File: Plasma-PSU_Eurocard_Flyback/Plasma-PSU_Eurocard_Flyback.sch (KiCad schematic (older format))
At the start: 21 parts

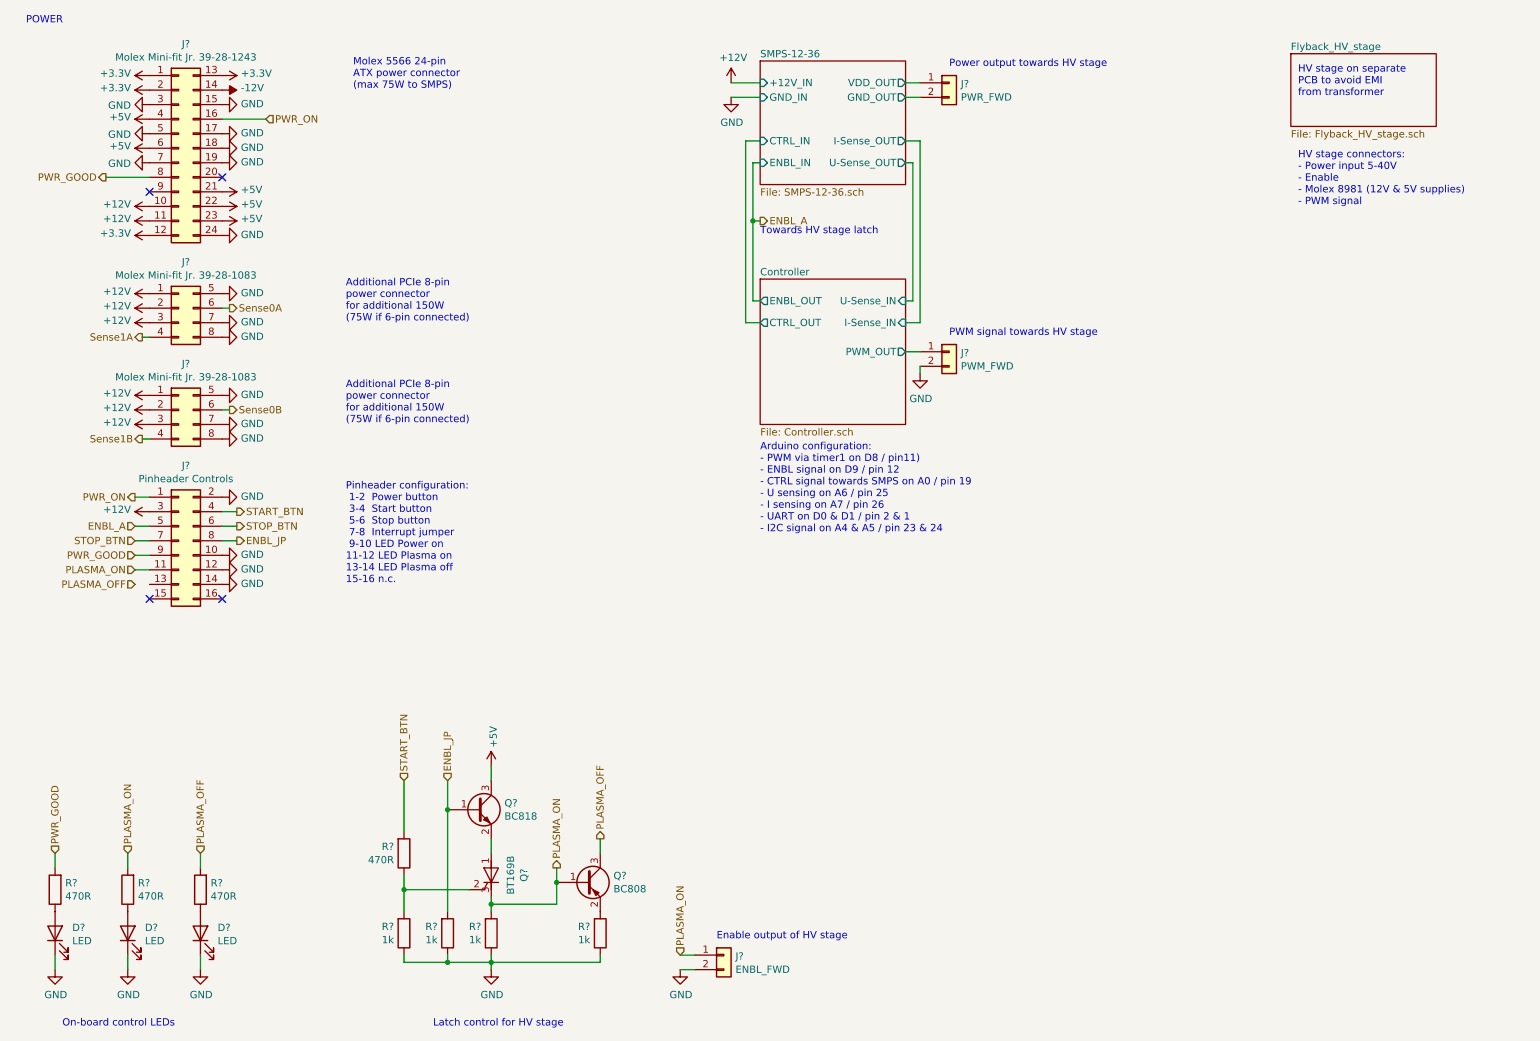
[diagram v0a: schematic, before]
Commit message: Block diagram, Connectivity, Isolation
- First page reservered for block diagram
- Connectors moved to separate sheet
- Opto-isolators for signal inputs on HV board
- Fuse added to SMPS
- Pinheader for Arduino pin-out, UART, I2C, SPI
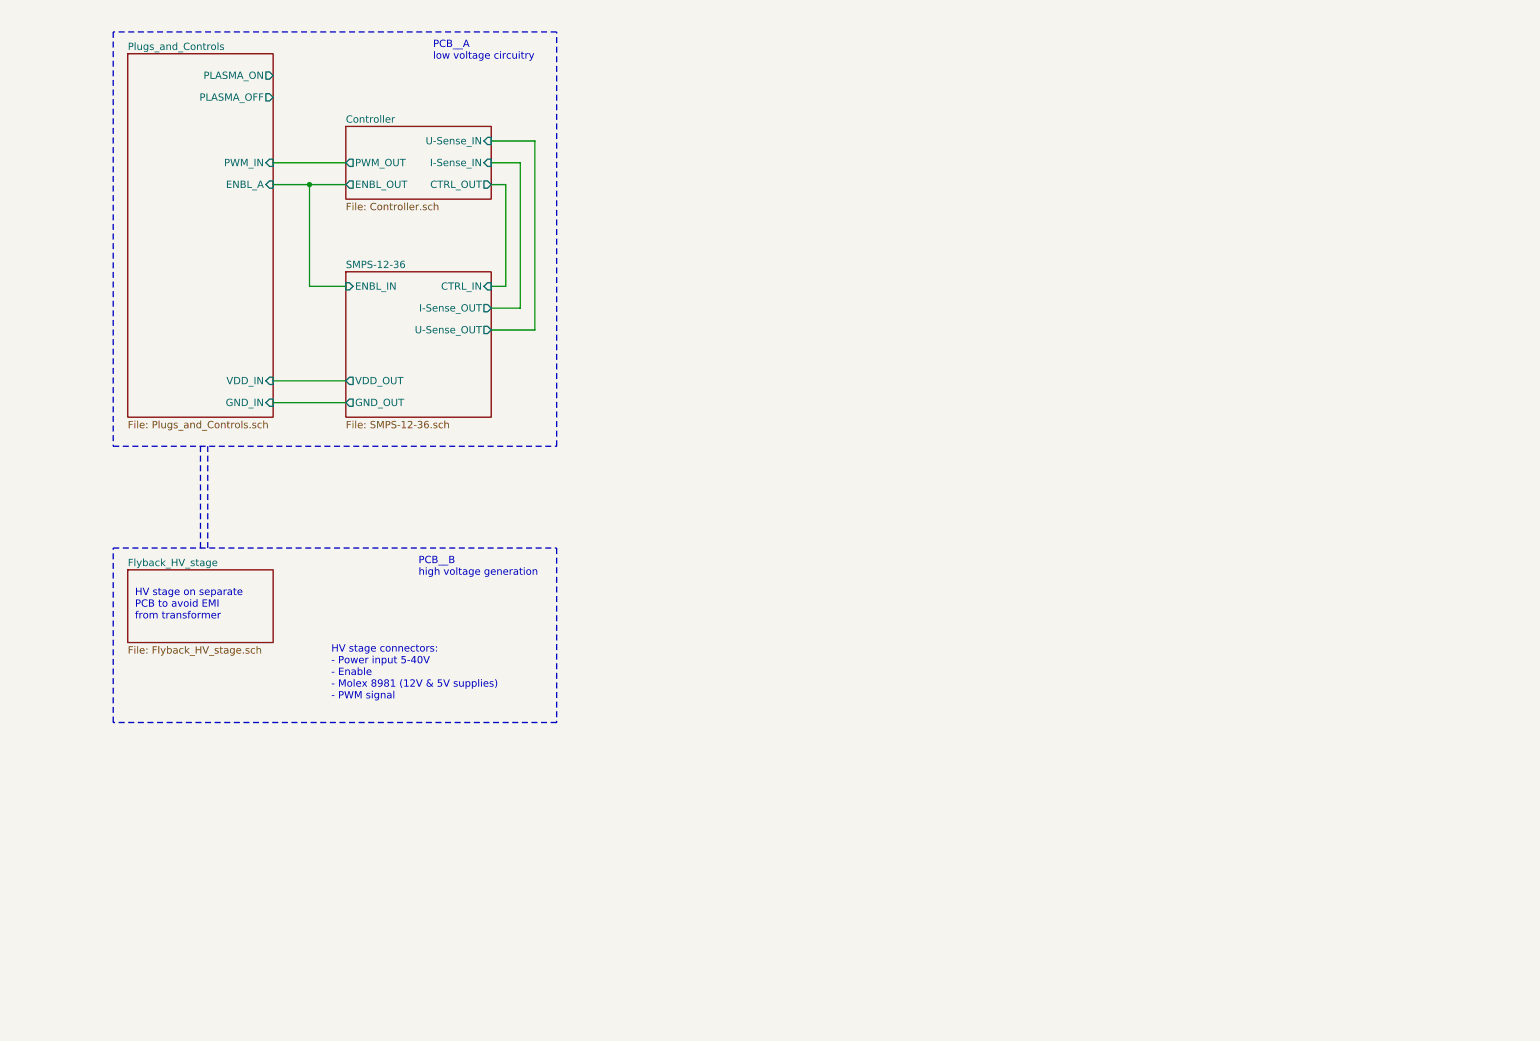
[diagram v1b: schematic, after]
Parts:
- removed D? (x3): LED, symbol Device:LED
- removed J?: Molex Mini-fit Jr. 39-28-1243, Connector_Molex:Molex_Mini-Fit_Jr_5566-24A_2x12_P4.20mm_Vertical, symbol Connector_Generic:Conn_02x12_Top_Bottom
- removed J? (x2): Molex Mini-fit Jr. 39-28-1083, Connector_Molex:Molex_Mini-Fit_Jr_5566-08A_2x04_P4.20mm_Vertical, symbol Connector_Generic:Conn_02x04_Top_Bottom
- removed J?: Pinheader Controls, Connector_PinHeader_2.54mm:PinHeader_2x08_P2.54mm_Vertical, symbol Connector_Generic:Conn_02x08_Odd_Even
- removed J?: PWR_FWD, symbol Connector_Generic:Conn_01x02
- removed J?: PWM_FWD, symbol Connector_Generic:Conn_01x02
- removed J?: ENBL_FWD, symbol Connector_Generic:Conn_01x02
- removed Q?: BT169B, Package_TO_SOT_THT:TO-92_Inline, symbol Triac_Thyristor:BT169B
- removed Q?: BC808, Package_TO_SOT_SMD:SOT-23, symbol Transistor_BJT:BC808
- removed Q?: BC818, Package_TO_SOT_SMD:SOT-23, symbol Transistor_BJT:BC818
- removed R? (x4): 1k, symbol Device:R
- removed R? (x4): 470R, symbol Device:R
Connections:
- no-connect marks 4 -> 0
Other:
- note added: "PCB__A\nlow voltage circuitry"
- note added: "PCB__B\nhigh voltage generation"
- note removed: "Additional PCIe 8-pin \npower connector\nfor additional 150W\n(75W if 6-pin connected)"
- note removed: "Arduino configuration:\n- PWM via timer1 on D8 / pin11)\n- ENBL signal on D9 / pin 12\n- CTRL signal towards SMPS on A0 / pin 19\n- U sensing on A6 / pin 25\n- I sensing on A7 / pin 26\n- UART on D0 & D1 / pin 2 & 1\n- I2C signal on A4 & A5 / pin 23 & 24"
- note removed: "Enable output of HV stage"
- note removed: "Latch control for HV stage"
- note removed: "Molex 5566 24-pin\nATX power connector\n(max 75W to SMPS)"
- note removed: "On-board control LEDs"
- note removed: "POWER"
- note removed: "PWM signal towards HV stage"
- note removed: "Pinheader configuration:\n 1-2 Power button\n 3-4 Start button\n 5-6 Stop button\n 7-8 Interrupt jumper\n 9-10 LED Power on\n11-12 LED Plasma on\n13-14 LED Plasma off\n15-16 n.c."
- note removed: "Power output towards HV stage"
- note removed: "Towards HV stage latch"

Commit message: Block diagram included
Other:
- note added: "12-36V\n0-15A"
- note added: "12V, 5V, GND"
- note added: "ARDUINO"
- note added: "ATX\nPOWER SUPPLY"
- note added: "BLOCK DIAGRAM"
- note added: "BOOST MODULE"
- note added: "DAC"
- note added: "FLYBACK\nDRIVER"
- note added: "HV FLYBACK\nTRANSFORMER"
- note added: "HV out"
- note added: "HV stage connectors:\n- Power input 5-40V\n- Enable\n- PWM signal"
- note added: "PCB A -- \nlow voltage circuits"
- note added: "PCB B -- \nhigh voltage generation"
- note added: "PWM (f,d%)"
- note added: "SOFT-START IC"
- note added: "sense U, I"
- note added: "set U"
- note removed: "HV stage connectors:\n- Power input 5-40V\n- Enable\n- Molex 8981 (12V & 5V supplies)\n- PWM signal"

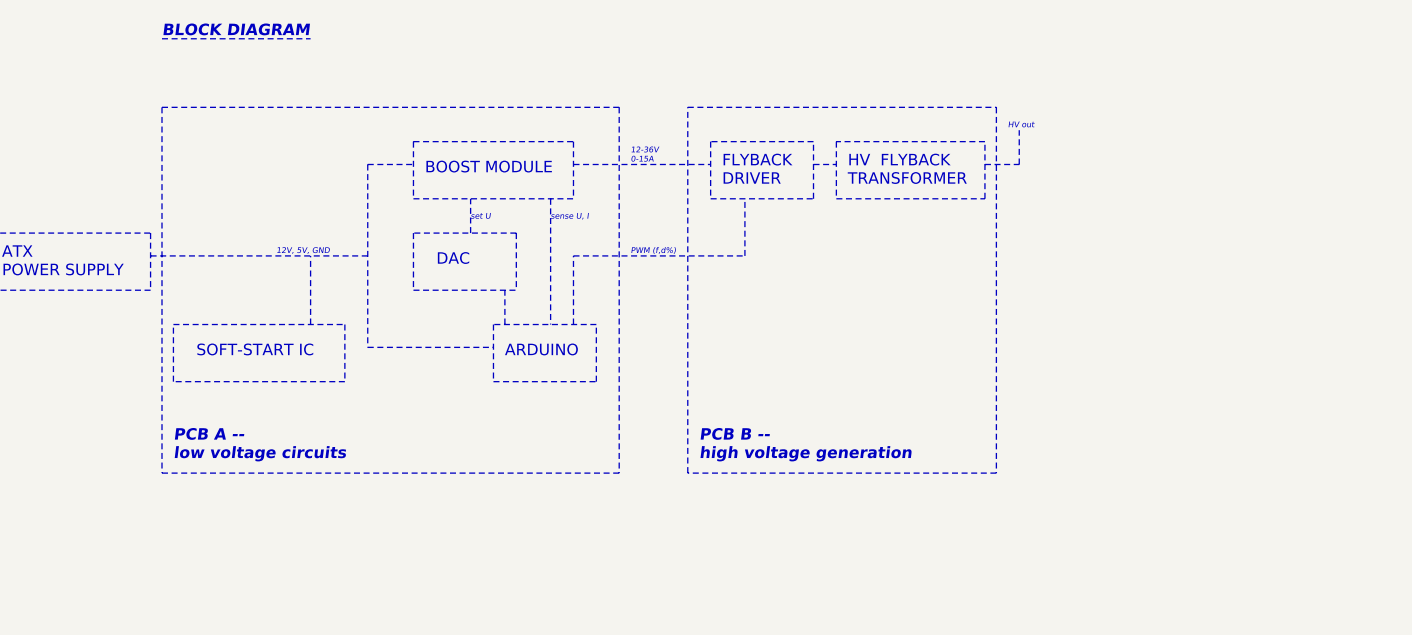
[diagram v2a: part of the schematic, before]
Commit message: Filters for sense signals
- RC filters on U-sense and I-sense included
- Block diagram refined
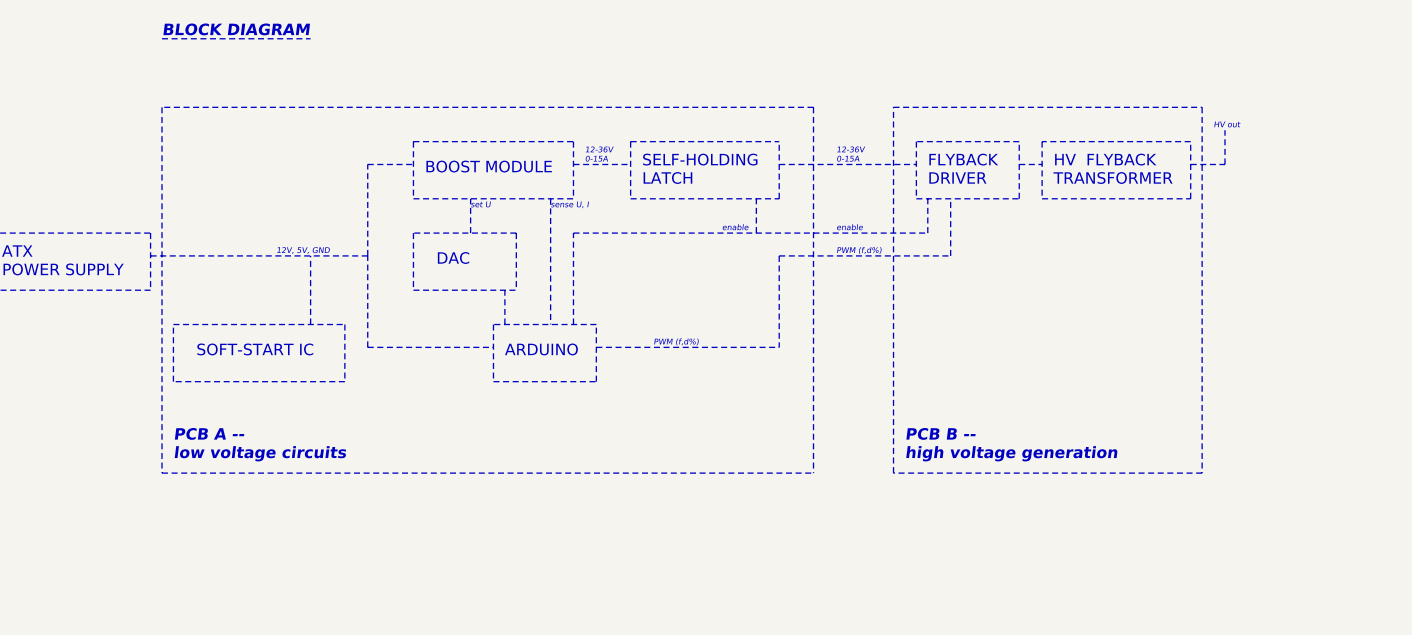
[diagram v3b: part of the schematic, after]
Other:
- note added: "SELF-HOLDING\nLATCH"
- note added: "enable"
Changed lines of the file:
@@
 Sheet 1 5
 Title "Plasma-PSU_Eurocard_Flyback"
-Date "2020-04-07"
-Rev "0.0.3"
+Date "2020-04-08"
+Rev "0.0.4"
 Comp "University of Ljubljana"
 Comment1 "Biotechnical faculty"
@@
 Text Notes 3100 2150 0    50   ~ 0
 DAC
-Text Notes 4350 1800 0    50   ~ 0
+Text Notes 5250 1800 0    50   ~ 0
 FLYBACK\nDRIVER
-Text Notes 4900 1800 0    50   ~ 0
+Text Notes 5800 1800 0    50   ~ 0
 HV  FLYBACK\nTRANSFORMER
 Wire Notes Line style solid
-	4850 1600 4850 1850
-Wire Notes Line style solid
-	4850 1850 5500 1850
-Wire Notes Line style solid
-	5500 1850 5500 1600
-Wire Notes Line style solid
-	5500 1600 4850 1600
-Wire Notes Line style solid
-	4300 1600 4300 1850
-Wire Notes Line style solid
-	4300 1850 4750 1850
-Wire Notes Line style solid
-	4750 1850 4750 1600
-Wire Notes Line style solid
-	4750 1600 4300 1600
-Wire Notes Line
-	4750 1700 4850 1700
+	5750 1600 5750 1850
+Wire Notes Line style solid
+	5750 1850 6400 1850
+Wire Notes Line style solid
+	6400 1850 6400 1600
+Wire Notes Line style solid
+	6400 1600 5750 1600
+Wire Notes Line style solid
+	5200 1600 5200 1850
+Wire Notes Line style solid
+	5200 1850 5650 1850
+Wire Notes Line style solid
+	5650 1850 5650 1600
+Wire Notes Line style solid
+	5650 1600 5200 1600
+Wire Notes Line width 10
+	5650 1700 5750 1700
 Wire Notes Line style solid
 	3450 2000 3450 2250
@@
 Wire Notes Line style solid
 	1150 2000 1850 2000
-Wire Notes Line
+Wire Notes Line width 10
 	2800 1700 3000 1700
 Wire Notes Line
-	2550 2400 2550 2100
-Wire Notes Line
 	3400 2400 3400 2250
 Wire Notes Line
 	3250 2000 3250 1850
-Text Notes 3250 1950 0    25   Italic 0
+Text Notes 3250 1900 0    25   Italic 0
 set U
 Wire Notes Line
 	3600 1850 3600 2400
-Text Notes 3600 1950 0    25   Italic 0
+Text Notes 3600 1900 0    25   Italic 0
 sense U, I
 Wire Notes Line
-	5500 1700 5650 1700
-Wire Notes Line
-	3700 1700 4300 1700
+	6400 1700 6550 1700
+Wire Notes Line width 10
+	4600 1700 5200 1700
+Text Notes 4850 1700 0    25   Italic 0
+12-36V\n0-15A
+Wire Notes Line
+	4600 2100 5350 2100
+Wire Notes Line
+	5350 2100 5350 1850
+Text Notes 4850 2100 0    25   Italic 0
+PWM (f,d%)
+Wire Notes Line
+	6550 1700 6550 1550
+Text Notes 6500 1550 0    25   Italic 0
+HV out
+Wire Notes Line
+	2800 2500 3350 2500
+Text Notes 1950 3000 0    50   Italic 10
+PCB A -- \nlow voltage circuits
+Wire Notes Line width 10
+	1850 2100 2800 2100
+Wire Notes Line style dotted
+	1900 1450 1900 3050
+Text Notes 5150 3000 0    50   Italic 10
+PCB B -- \nhigh voltage generation
+Wire Notes Line style dotted
+	5100 1450 6450 1450
+Wire Notes Line style dotted
+	6450 1450 6450 3050
+Wire Notes Line style dotted
+	6450 3050 5100 3050
+Wire Notes Line style dotted
+	5100 3050 5100 1450
+Wire Notes Line style dotted
+	4750 1450 4750 3050
+Text Notes 1900 1150 0    50   Italic 10
+BLOCK DIAGRAM
+Wire Notes Line style solid
+	1900 1150 2550 1150
+Text Notes 4000 1800 0    50   ~ 0
+SELF-HOLDING\nLATCH
+Wire Notes Line style solid
+	3950 1600 3950 1850
+Wire Notes Line style solid
+	4600 1850 4600 1600
+Wire Notes Line style solid
+	3950 1850 4600 1850
+Wire Notes Line style solid
+	3950 1600 4600 1600
+Text Notes 3750 1700 0    25   Italic 0
+12-36V\n0-15A
+Text Notes 4050 2500 0    25   Italic 0
+PWM (f,d%)
+Wire Notes Line
+	3800 2500 4600 2500
+Wire Notes Line
+	4600 2100 4600 2500
+Wire Notes Line
+	3700 2400 3700 2000
+Wire Notes Line
+	3700 2000 5250 2000
+Wire Notes Line
+	5250 2000 5250 1850
+Wire Notes Line
+	4500 2000 4500 1850
+Text Notes 4350 2000 0    25   Italic 0
+enable
+Text Notes 4850 2000 0    25   Italic 0
+enable
+Wire Notes Line style dotted
+	4750 1450 1900 1450
+Wire Notes Line style dotted
+	1900 3050 4750 3050
+Wire Notes Line width 10
+	3700 1700 3950 1700
 Text Notes 2400 2100 0    25   Italic 0
 12V, 5V, GND
-Text Notes 3950 1700 0    25   Italic 0
-12-36V\n0-15A
-Wire Notes Line
-	3700 2400 3700 2100
-Wire Notes Line
-	3700 2100 4450 2100
-Wire Notes Line
-	4450 2100 4450 1850
-Text Notes 3950 2100 0    25   Italic 0
-PWM (f,d%)
-Wire Notes Line
-	5650 1700 5650 1550
-Text Notes 5600 1550 0    25   Italic 0
-HV out
-Wire Notes Line
-	2800 2500 3350 2500
-Wire Notes Line
-	2800 1700 2800 2500
-Text Notes 1950 3000 0    50   Italic 10
-PCB A -- \nlow voltage circuits
-Wire Notes Line
-	1850 2100 2800 2100
-Wire Notes Line style dotted
-	3900 1450 1900 1450
-Wire Notes Line style dotted
-	1900 1450 1900 3050
-Wire Notes Line style dotted
-	1900 3050 3900 3050
-Text Notes 4250 3000 0    50   Italic 10
-PCB B -- \nhigh voltage generation
-Wire Notes Line style dotted
-	4200 1450 5550 1450
-Wire Notes Line style dotted
-	5550 1450 5550 3050
-Wire Notes Line style dotted
-	5550 3050 4200 3050
-Wire Notes Line style dotted
-	4200 3050 4200 1450
-Wire Notes Line style dotted
-	3900 1450 3900 3050
-Text Notes 1900 1150 0    50   Italic 10
-BLOCK DIAGRAM
-Wire Notes Line style solid
-	1900 1150 2550 1150
+Wire Notes Line
+	2550 2400 2550 2100
+Wire Notes Line width 10
+	2800 2100 2800 1700
+Wire Notes Line
+	2800 2500 2800 2100
 $EndSCHEMATC
